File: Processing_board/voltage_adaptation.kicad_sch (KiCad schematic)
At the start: 11 parts, among them IC1 DMP3056LSS-13

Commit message: the 2nd (hopefully final) version of circuit diagram
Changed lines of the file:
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@@
 	(text "Schotky Diode (Vf ~ 0.4V)\n"
 		(exclude_from_sim no)
-		(at 181.102 115.062 0)
-		(effects
-			(font
-				(size 1.27 1.27)
-			)
-		)
-	)
-	(text "Schotky Diode"
-		(exclude_from_sim no)
-		(at 117.856 113.03 0)
+		(at 113.03 109.982 0)
 		(effects
 			(font
@@
 		(pts
 			(xy 177.8 130.81) (xy 177.8 124.46)
+		)
+		(stroke
+			(width 0)
+			(type default)
+		)
+	)
+	(wire
+		(pts
+			(xy 259.08 146.05) (xy 259.08 147.32)
 		)
 		(stroke
@@
 		(on_board yes)
 		(dnp no)
-		(fields_autoplaced yes)
 		(property "Reference" "LD1117DT18TR2"
 			(at 230.505 99.06 0)

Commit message: added reset button
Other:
- company: (none) -> N-Pulse
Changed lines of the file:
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@@
 	(generator_version "9.0")
 	(paper "A4")
+	(title_block
+		(company "N-Pulse")
+	)
 	(text "LDO->3.3V"
 		(exclude_from_sim no)

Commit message: addressed all reviews except the LDO 5V
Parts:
- added D4: IN_S42BT LED, symbol Device:LED
- added R6: 100R, symbol Device:R_Small
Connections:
- net 3.3V: now also R6.2
- net GND: now also D4.1 (K)
- new net: D4.2 (A), R6.1
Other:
- note added: "PWR LED"
- note added: "This should sink ~10mA Is it too much ? Is it a problem ? How to calculate my current budget ?"
- moved on the sheet: C10, C11, C12, C9, IC1, LD1117DT18TR2, LD1117S33TR2, R2

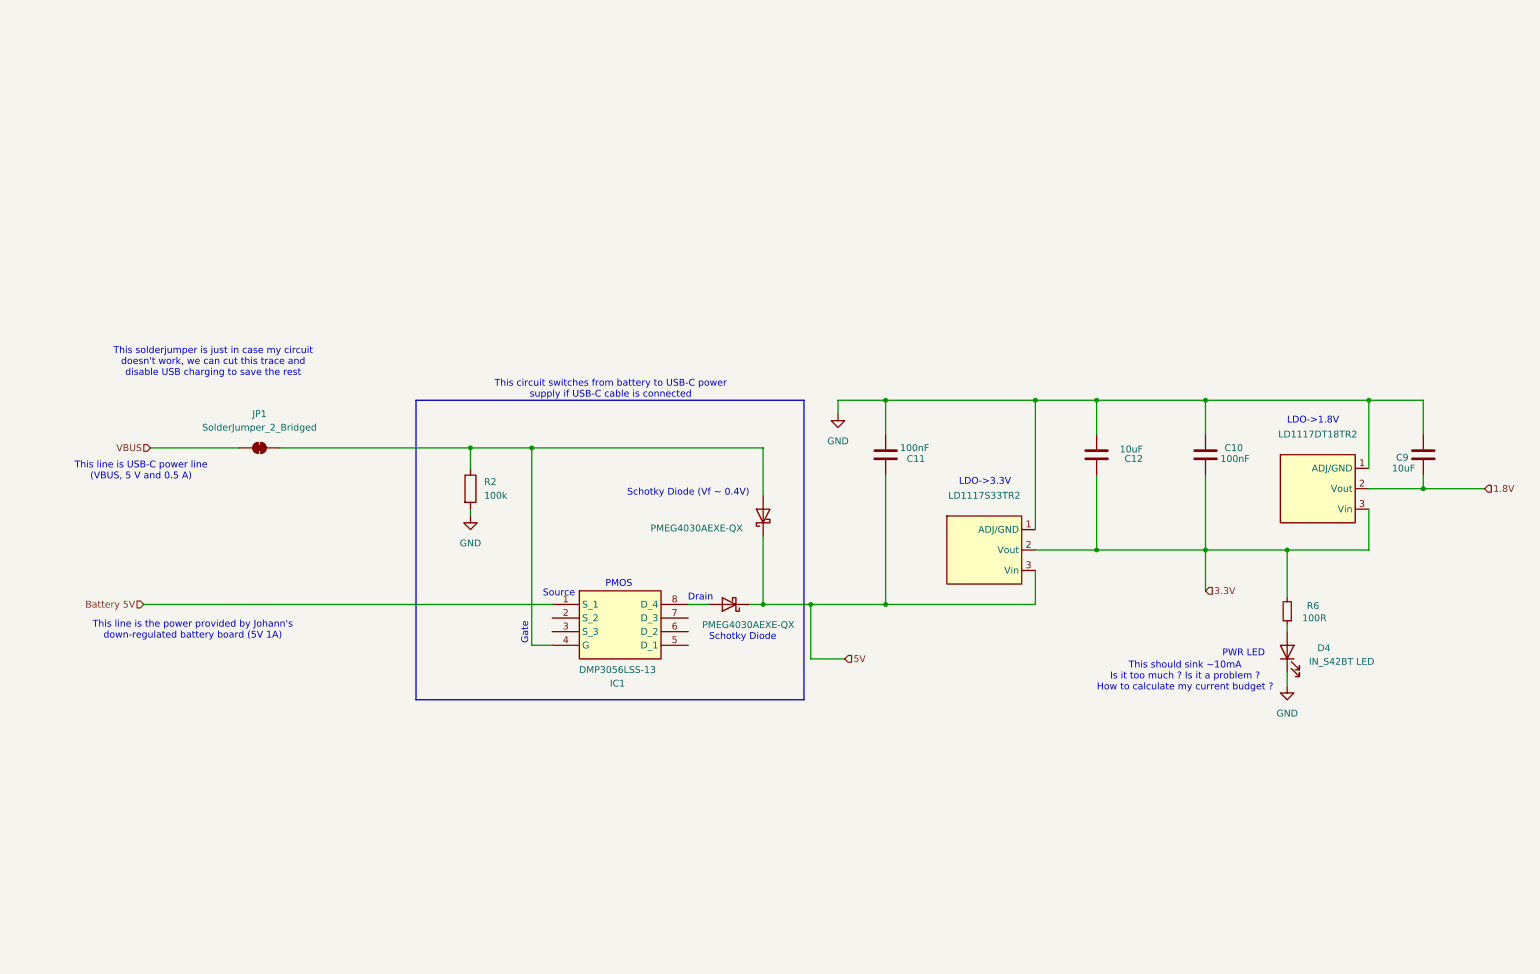
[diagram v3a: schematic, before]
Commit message: 5V LDO and jumper cables to handle 2S battery OR johann's powerline
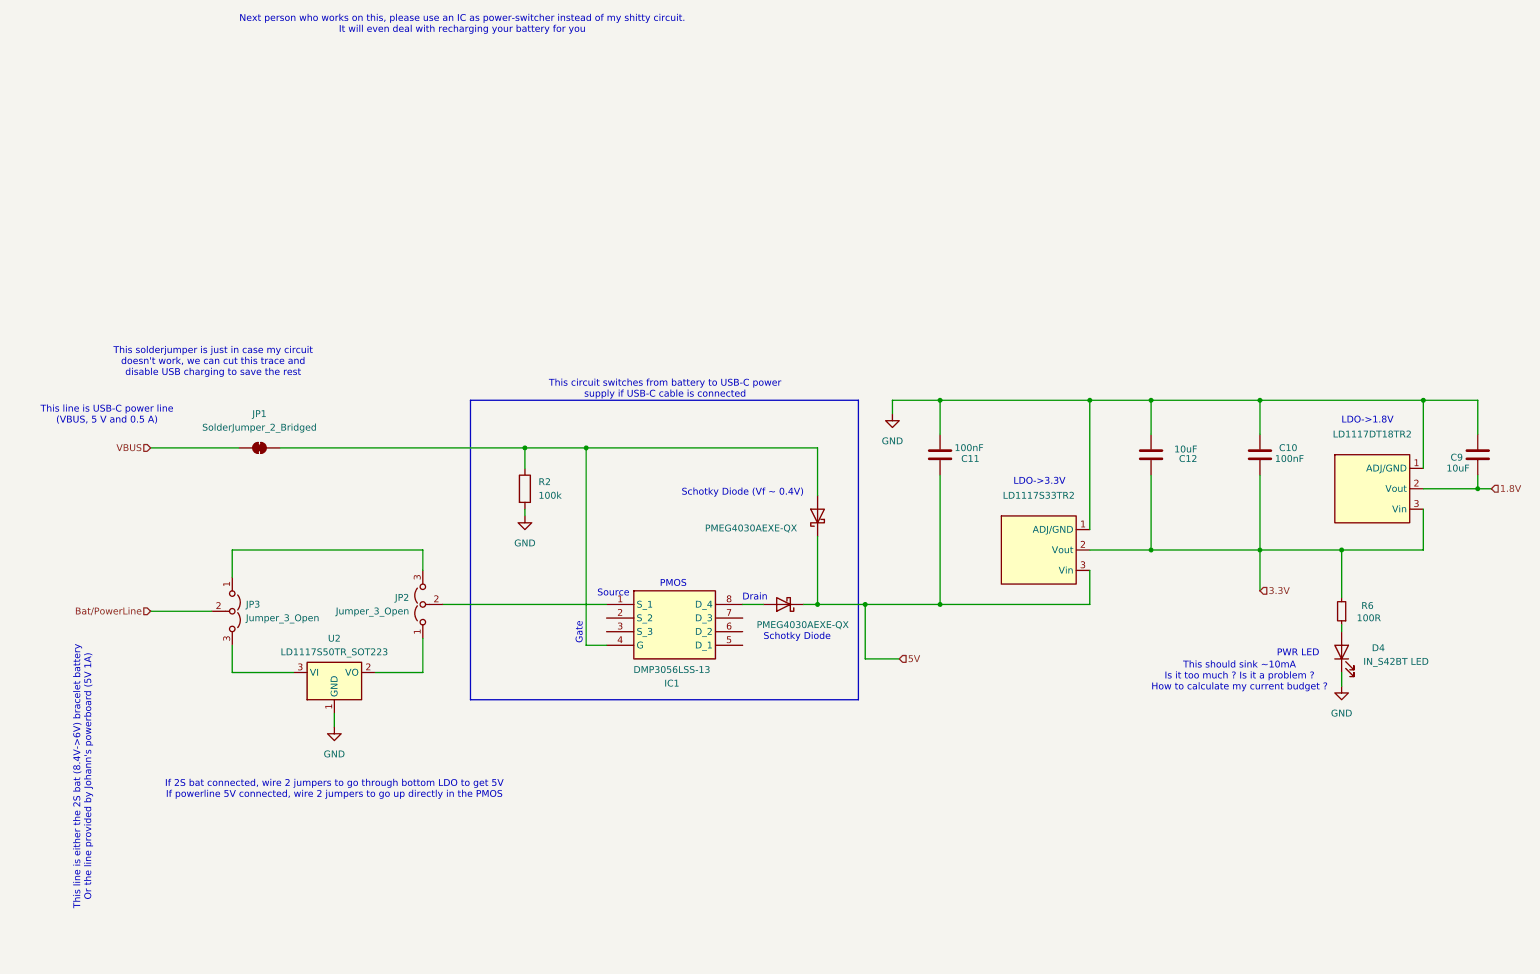
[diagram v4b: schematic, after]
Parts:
- added JP2, JP3: Jumper_3_Open, symbol Jumper:Jumper_3_Open
- added U2: LD1117S50TR_SOT223, Package_TO_SOT_SMD:SOT-223-3_TabPin2, symbol Regulator_Linear:LD1117S50TR_SOT223
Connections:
- net GND: now also U2.1 (GND)
- net Battery 5V: no longer names the net of IC1.1 (S_1)
- net Battery 5V: now also JP2.2 (C)
- new net: JP2.3 (B), JP3.1 (A)
- new net: JP3.3 (B), U2.3 (VI)
- new net: JP2.1 (A), U2.2 (VO)
- new net Bat/PowerLine: JP3.2 (C)
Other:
- note added: "If 2S bat connected, wire 2 jumpers to go through bottom LDO to get 5V If powerline 5V connected, wire 2 jumpers to go up directly in the PMOS"
- note added: "Next person who works on this, please use an IC as power-switcher instead of my shitty circuit. It will even deal with recharging your battery for you"
- note added: "This line is either the 2S bat (8.4V->6V) bracelet battery Or the line provided by Johann's powerboard (5V 1A)"
- note removed: "This line is the power provided by Johann's down-regulated battery board (5V 1A)"
- moved on the sheet: C10, C11, C12, C9, D4, IC1, LD1117DT18TR2, LD1117S33TR2, R2, R6

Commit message: added all footprints, ready (?) to design PCB
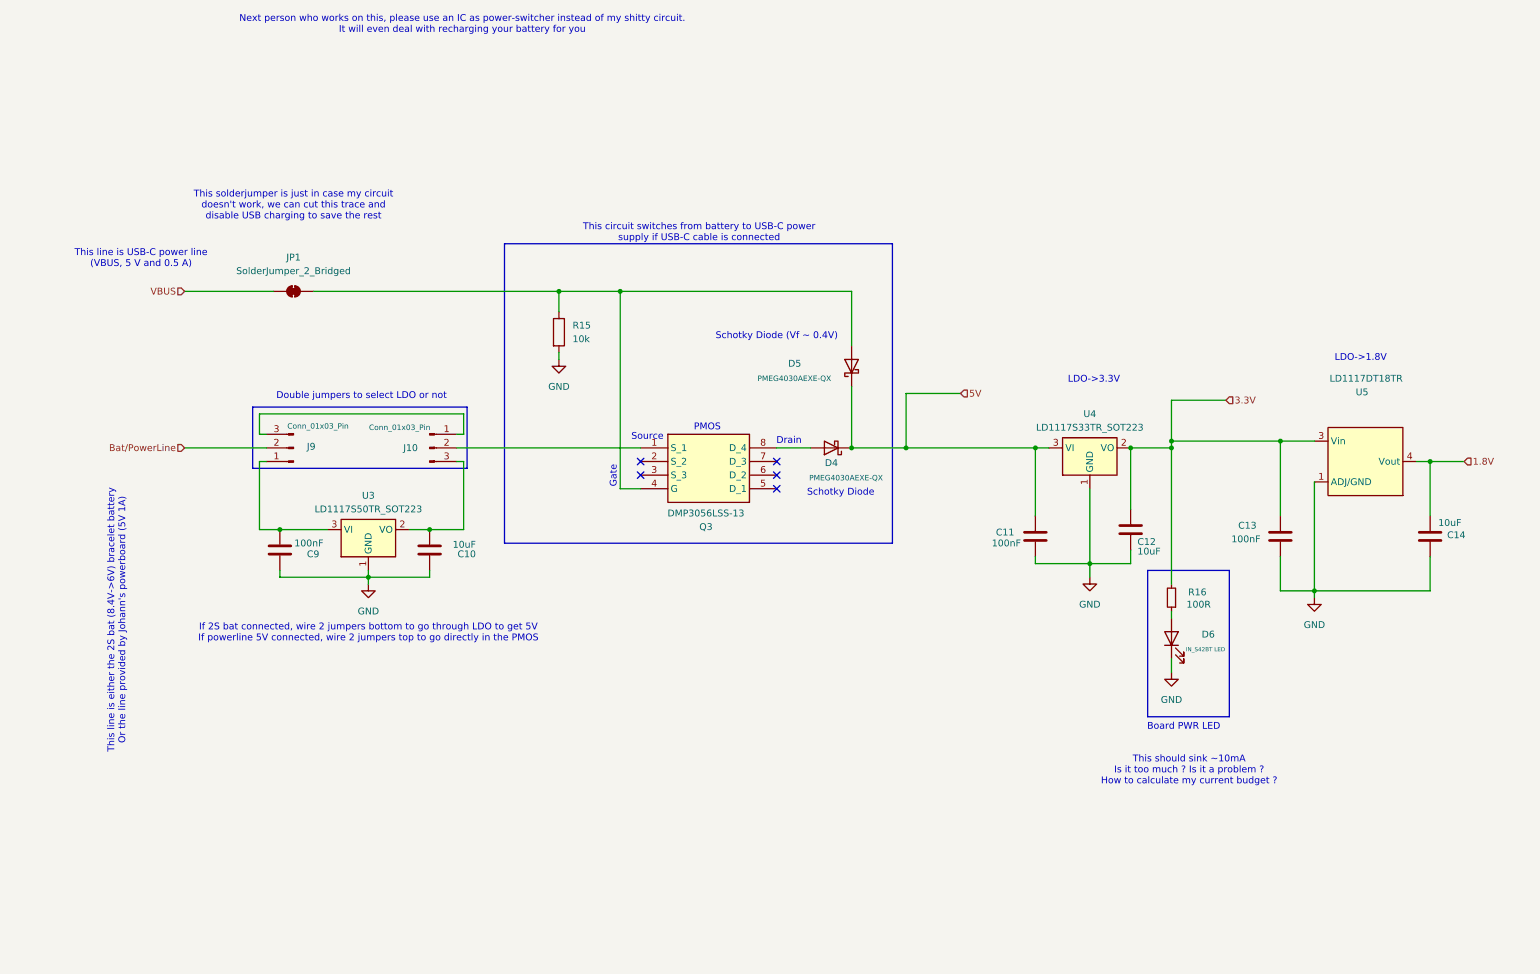
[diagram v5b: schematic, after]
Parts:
- removed D7: PMEG4030AEXE-QX, PMEG4030AEXEQX, symbol Device:D_Schottky
- removed JP2, JP3: Jumper_3_Open, symbol Jumper:Jumper_3_Open
- removed LD1117S33TR2: ~, symbol Custom_Symbol_Library_Npulse:LD1117S33TR (pack SOT-223)
- added C10: 10uF, Capacitor_SMD:C_0402_1005Metric, symbol Device:C
- added C9: 100nF, Capacitor_SMD:C_0402_1005Metric, symbol Device:C
- added D4: PMEG4030AEXE-QX, PMEG4030AEXE-QX:PMEG4030AEXEQX, symbol Device:D_Schottky
- added J10, J9: Conn_01x03_Pin, Connector_PinHeader_2.54mm:PinHeader_1x03_P2.54mm_Vertical_SMD_Pin1Left, symbol Connector:Conn_01x03_Pin
- added U4: LD1117S33TR_SOT223, Package_TO_SOT_SMD:SOT-223-3_TabPin2, symbol Regulator_Linear:LD1117S33TR_SOT223
- C11, C12: footprint (none) -> Capacitor_SMD:C_0402_1005Metric
- C13: renamed from C10; footprint (none) -> Capacitor_SMD:C_0402_1005Metric
- C14: renamed from C9; footprint (none) -> Capacitor_SMD:C_0402_1005Metric
- D5: renamed from D6; footprint PMEG4030AEXEQX -> PMEG4030AEXE-QX:PMEG4030AEXEQX
- D6: renamed from D4; footprint (none) -> LED_SMD:LED_0402_1005Metric
- JP1: footprint (none) -> Jumper:SolderJumper-2_P1.3mm_Bridged2Bar_RoundedPad1.0x1.5mm
- Q3: renamed from IC1; footprint SOIC127P600X170-8N -> DMP3056LSS-13:SOIC127P600X170-8N
- R15: renamed from R2; value 100k -> 10k; footprint (none) -> Resistor_SMD:R_0402_1005Metric
- R16: renamed from R6; footprint (none) -> Resistor_SMD:R_0402_1005Metric
- U5: renamed from LD1117DT18TR2; value ~ -> LD1117DT18TR; footprint (none) -> LD1117DT18TR:TO228P972X240-3N
- renumbered U2 to U3
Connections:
- net 1.8V: now also U5.4 (Vout); no longer U5.2 (Vout)
- net 3.3V: now also C13.1, U4.2 (VO); no longer C13.2
- net 5V: now also D5.3 (K), D4.1 (K), D4.3 (K), U4.3 (VI)
- net Bat/PowerLine: now also J9.2 (Pin_2)
- net GND: now also C13.2, C10.1, C9.1, U4.1 (GND); no longer C13.1
- net at U3.3 (VI): now also C9.2, J9.1 (Pin_1)
- net at Q3.1 (S_1): now also J10.2 (Pin_2)
- net at Q3.8 (D_4): now also D4.2 (A)
- net at U3.2 (VO): now also C10.2, J10.3 (Pin_3)
- new net: J10.1 (Pin_1), J9.3 (Pin_3)
- no-connect marks 0 -> 5
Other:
- note added: "Board PWR LED"
- note added: "Double jumpers to select LDO or not"
- note added: "If 2S bat connected, wire 2 jumpers bottom to go through LDO to get 5V If powerline 5V connected, wire 2 jumpers top to go directly in the PMOS"
- note removed: "If 2S bat connected, wire 2 jumpers to go through bottom LDO to get 5V If powerline 5V connected, wire 2 jumpers to go up directly in the PMOS"
- note removed: "PWR LED"
- moved on the sheet: C11, C12, C13, C14, D6, JP1, Q3, R15, R16, U3, U5

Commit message: first draft of PCB almost done
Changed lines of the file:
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@@
+	(wire
+		(pts
+			(xy 86.36 101.6) (xy 120.65 101.6)
+		)
+		(stroke
+			(width 0)
+			(type default)
+		)
+	)
 	(wire
 		(pts
@@
 	(wire
 		(pts
+			(xy 86.36 104.14) (xy 87.63 104.14)
+		)
+		(stroke
+			(width 0)
+			(type default)
+		)
+	)
+	(wire
+		(pts
 			(xy 87.63 95.25) (xy 87.63 99.06)
 		)
@@
 	(wire
 		(pts
-			(xy 86.36 101.6) (xy 120.65 101.6)
-		)
-		(stroke
-			(width 0)
-			(type default)
-		)
-	)
-	(wire
-		(pts
 			(xy 212.09 123.19) (xy 212.09 120.65)
 		)
@@
 	(wire
 		(pts
+			(xy 86.36 99.06) (xy 87.63 99.06)
+		)
+		(stroke
+			(width 0)
+			(type default)
+		)
+	)
+	(wire
+		(pts
 			(xy 194.31 101.6) (xy 194.31 114.3)
 		)
@@
 		(pts
 			(xy 49.53 116.84) (xy 53.34 116.84)
-		)
-		(stroke
-			(width 0)
-			(type default)
-		)
-	)
-	(wire
-		(pts
-			(xy 87.63 99.06) (xy 86.36 99.06)
-		)
-		(stroke
-			(width 0)
-			(type default)
-		)
-	)
-	(wire
-		(pts
-			(xy 87.63 104.14) (xy 86.36 104.14)
 		)
 		(stroke
@@
 		(dnp no)
 		(property "Reference" "J10"
-			(at 77.724 101.6 0)
+			(at 77.978 101.6 0)
 			(effects
 				(font
@@
 		)
 		(property "Value" "Conn_01x03_Pin"
-			(at 75.692 97.79 0)
-			(effects
-				(font
+			(at 77.724 96.774 0)
+			(effects
+				(font

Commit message: more minor cleanup
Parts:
- added TP5: 5V, TestPoint:TestPoint_Pad_D1.0mm, symbol Connector:TestPoint
- added TP6: 5V-, TestPoint:TestPoint_Pad_D1.0mm, symbol Connector:TestPoint
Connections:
- net 5V: now also TP6.1
- net at C10.2, J10.3 (Pin_3), U3.2 (VO): now also TP5.1
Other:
- note added: "One test point before (5V) and one after (5V-) transistor and diodes to check voltage drop"
- moved on the sheet: C13, C14, U5

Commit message: more cleanup
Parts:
- renumbered C12 to C100, C13 to C106, C14 to C109, C9 to C59, C10 to C66, C11 to C95, D6 to D12, D4 to D8, D5 to D9, J9 to J19, J10 to J20, JP1 to JP2, Q3 to Q5, R15 to R27, R16 to R35, TP5 to TP16, TP6 to TP19, U3 to U12, U4 to U17, U5 to U18
